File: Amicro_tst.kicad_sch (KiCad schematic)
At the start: 19 parts, among them J1 Conn_01x04_Female, J2 Conn_01x05_Female, J3 Conn_01x04_Female, SW1 SW_Push, U1 ATmega328-P, U2 24LC512, Y1 Crystal

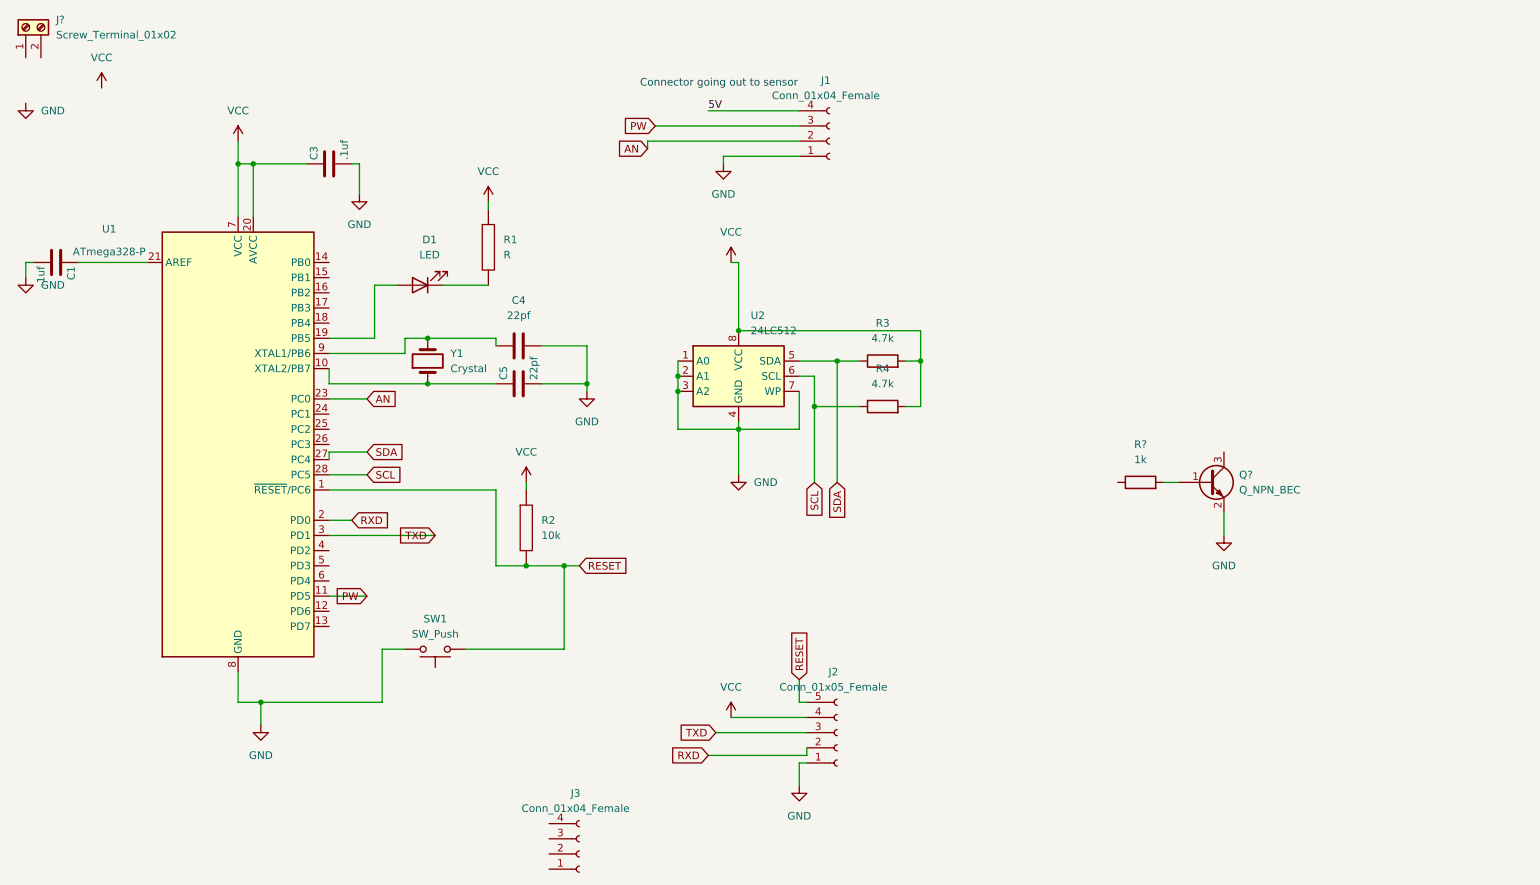
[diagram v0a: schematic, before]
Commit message: redid lost work/testpoints
Redid lost work that didnt save, still need to find footprints for transistors
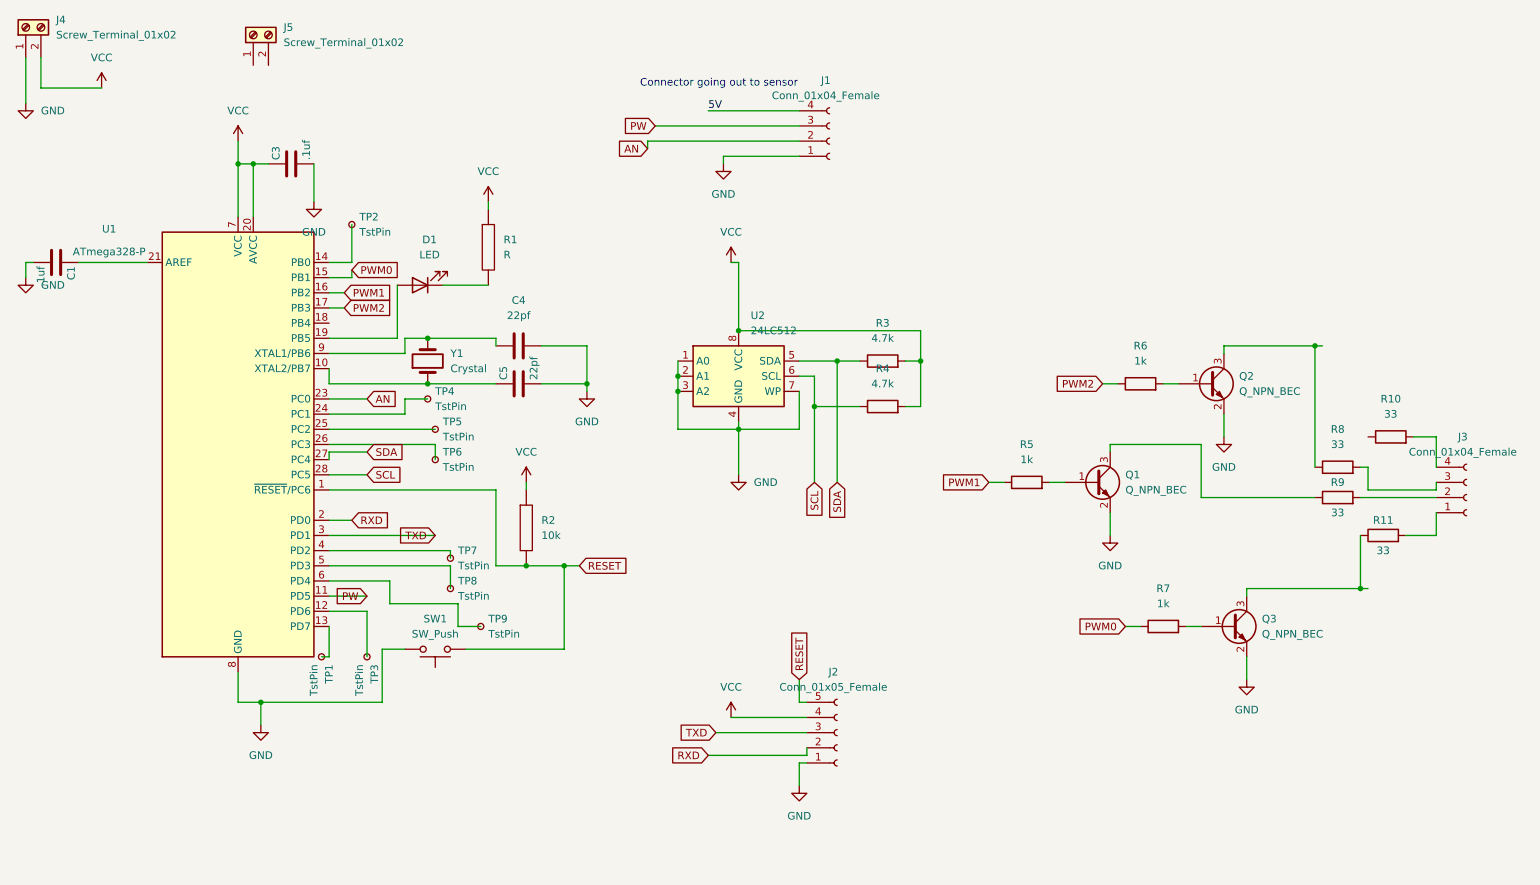
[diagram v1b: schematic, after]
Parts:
- added J5: Screw_Terminal_01x02, symbol Connector:Screw_Terminal_01x02
- added Q2, Q3: Q_NPN_BEC, symbol Device:Q_NPN_BEC
- added R10, R11, R8, R9: 33, Resistor_SMD:R_0402_1005Metric, symbol Device:R
- added R6, R7: 1k, Resistor_SMD:R_0402_1005Metric, symbol Device:R
- added TP1, TP2, TP3, TP4, TP5, TP6, TP7, TP8, TP9: TstPin, TestPoint:TestPoint_THTPad_1.0x1.0mm_Drill0.5mm, symbol Connector:TestPoint_Small
- J4: renamed from J?; footprint (none) -> TerminalBlock_4Ucon:TerminalBlock_4Ucon_1x02_P3.50mm_Vertical
- gave numbers to parts that had none: 2
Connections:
- net GND: now also J4.1 (Pin_1), Q2.2 (E), Q3.2 (E)
- net VCC: now also J4.2 (Pin_2)
- net at Q1.3 (C): now also R9.1
- net PWM1: now reaches R5.1
- net PWM1: now also U1.16 (PB2)
- net at U1.12 (PD6): now also TP3.1
- net at U1.13 (PD7): now also TP1.1
- net at U1.14 (PB0): now also TP2.1
- net PWM0: now reaches U1.15 (PB1)
- net PWM0: now also R7.1
- net PWM2: now reaches U1.17 (PB3)
- net PWM2: now also R6.1
- net at U1.24 (PC1): now also TP4.1
- net at U1.25 (PC2): now also TP5.1
- net at U1.26 (PC3): now also TP6.1
- net at U1.4 (PD2): now also TP7.1
- net at U1.5 (PD3): now also TP8.1
- net at U1.6 (PD4): now also TP9.1
- net at J3.1 (Pin_1): now also R11.2
- net at J3.2 (Pin_2): now also R9.2
- net at J3.3 (Pin_3): now also R8.2
- net at J3.4 (Pin_4): now also R10.2
- new net: Q2.3 (C), R8.1
- new net: Q2.1 (B), R6.2
- new net: Q3.1 (B), R7.2
- new net: Q3.3 (C), R11.1
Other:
- moved on the sheet: C3, J3, Q1, R5

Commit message: transistor footprints
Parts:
- J1: footprint Connector_PinSocket_1.00mm:PinSocket_1x05_P1.00mm_Vertical -> Connector_JST:JST_EH_S4B-EH_1x04_P2.50mm_Horizontal
- Q1: footprint (none) -> Package_TO_SOT_SMD:SC-59_Handsoldering
- Q2, Q3: footprint (none) -> TO_SOT_Packages_SMD:SC-59_Handsoldering
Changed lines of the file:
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@@
       (effects (font (size 1.27 1.27)) (justify left))
     )
-    (property "Footprint" "" (id 2) (at 214.63 116.84 0)
+    (property "Footprint" "Package_TO_SOT_SMD:SC-59_Handsoldering" (id 2) (at 214.63 116.84 0)
       (effects (font (size 1.27 1.27)) hide)
     )
@@
     (property "Reference" "J1" (id 0) (at 164.465 52.07 0))
     (property "Value" "Conn_01x04_Female" (id 1) (at 164.465 54.61 0))
-    (property "Footprint" "Connector_PinSocket_1.00mm:PinSocket_1x05_P1.00mm_Vertical" (id 2) (at 165.1 62.23 0)
+    (property "Footprint" "Connector_JST:JST_EH_S4B-EH_1x04_P2.50mm_Horizontal" (id 2) (at 165.1 62.23 0)
       (effects (font (size 1.27 1.27)) hide)
     )
@@
       (effects (font (size 1.27 1.27)) (justify left))
     )
-    (property "Footprint" "" (id 2) (at 233.68 100.33 0)
+    (property "Footprint" "TO_SOT_Packages_SMD:SC-59_Handsoldering" (id 2) (at 233.68 100.33 0)
       (effects (font (size 1.27 1.27)) hide)
     )
@@
       (effects (font (size 1.27 1.27)) (justify left))
     )
-    (property "Footprint" "" (id 2) (at 237.49 140.97 0)
+    (property "Footprint" "TO_SOT_Packages_SMD:SC-59_Handsoldering" (id 2) (at 237.49 140.97 0)
       (effects (font (size 1.27 1.27)) hide)
     )
@@
     )
     (path "/5188af90-2c2e-4efc-b1a8-f03acba966ff"
-      (reference "J1") (unit 1) (value "Conn_01x04_Female") (footprint "Connector_PinSocket_1.00mm:PinSocket_1x05_P1.00mm_Vertical")
+      (reference "J1") (unit 1) (value "Conn_01x04_Female") (footprint "Connector_JST:JST_EH_S4B-EH_1x04_P2.50mm_Horizontal")
     )
     (path "/fabc0f20-6748-4256-8270-8d8c1ba7f1db"
@@
     )
     (path "/2040b5f2-deb5-43fd-af37-1d21e87e6c5d"
-      (reference "Q1") (unit 1) (value "Q_NPN_BEC") (footprint "")
+      (reference "Q1") (unit 1) (value "Q_NPN_BEC") (footprint "Package_TO_SOT_SMD:SC-59_Handsoldering")
     )
     (path "/554d6924-f0a1-44e8-9c6e-2df61b13682e"
-      (reference "Q2") (unit 1) (value "Q_NPN_BEC") (footprint "")
+      (reference "Q2") (unit 1) (value "Q_NPN_BEC") (footprint "TO_SOT_Packages_SMD:SC-59_Handsoldering")
     )
     (path "/c9e48f35-9002-4ee0-bbbf-ca80e2ff2954"
-      (reference "Q3") (unit 1) (value "Q_NPN_BEC") (footprint "")
+      (reference "Q3") (unit 1) (value "Q_NPN_BEC") (footprint "TO_SOT_Packages_SMD:SC-59_Handsoldering")
     )
     (path "/2719589e-6f3e-41f2-ae58-0c107b009320"

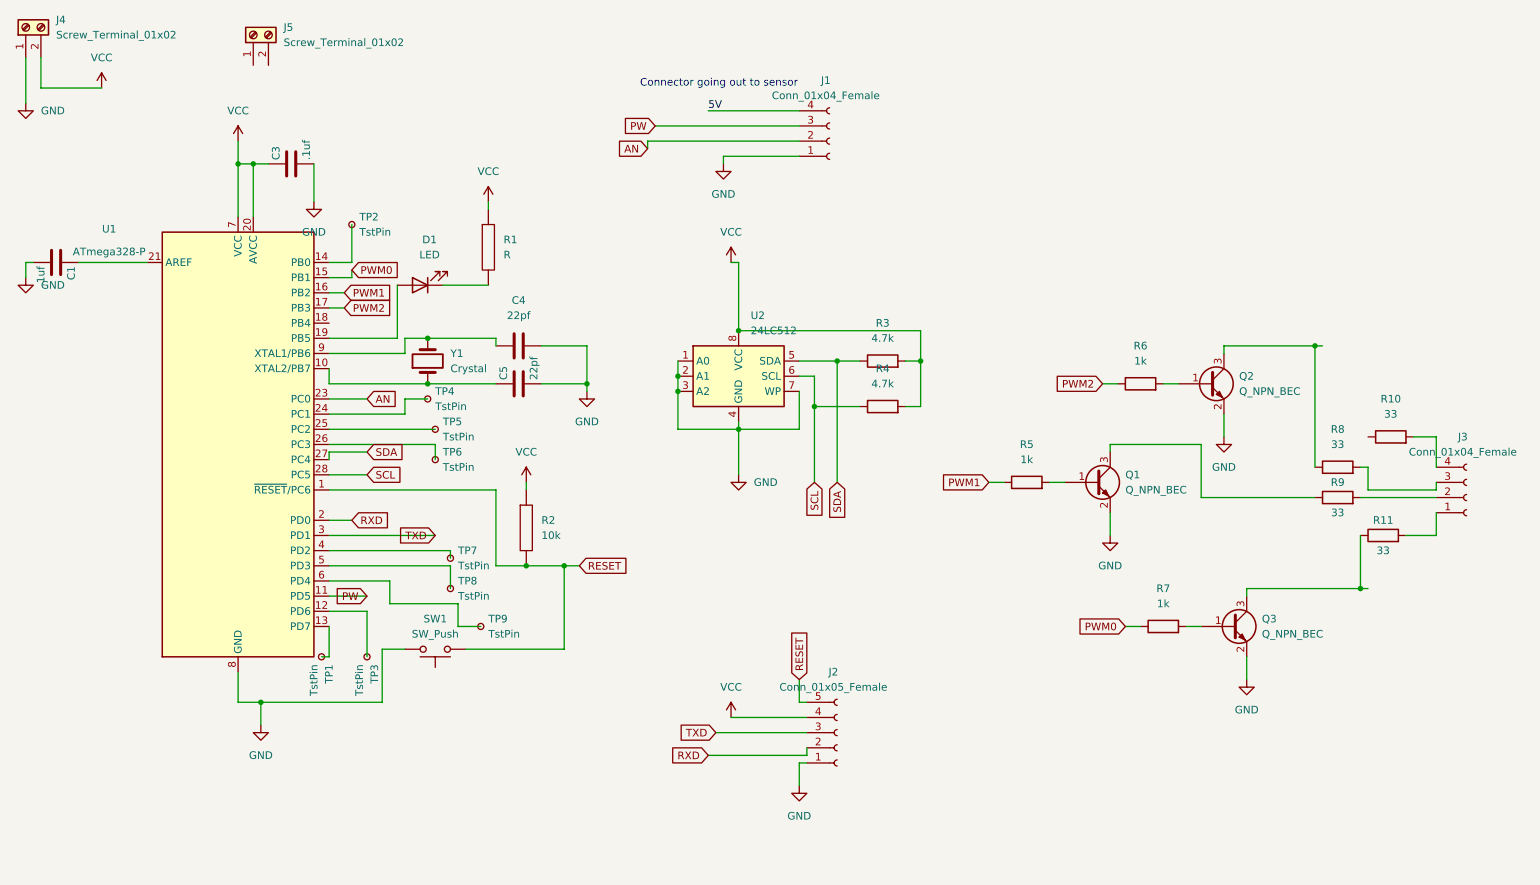
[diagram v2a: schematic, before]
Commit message: Changed Footprints & Board Size
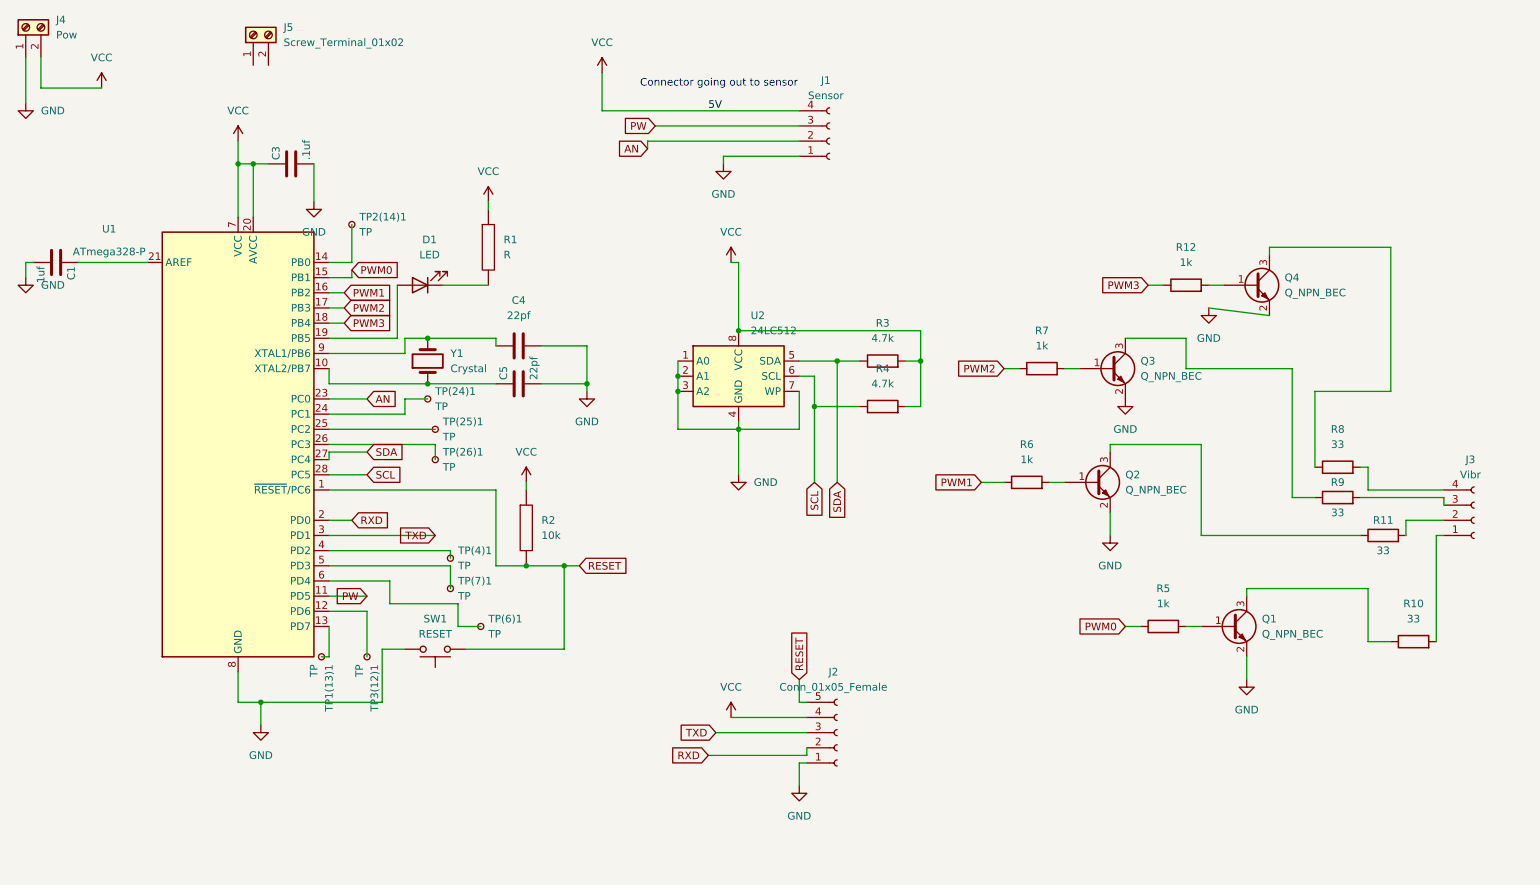
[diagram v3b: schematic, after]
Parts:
- added Q4: Q_NPN_BEC, Package_TO_SOT_SMD:SC-59_Handsoldering, symbol Device:Q_NPN_BEC
- added R12: 1k, Resistor_SMD:R_0402_1005Metric, symbol Device:R
- J1: value Conn_01x04_Female -> Sensor
- J3: value Conn_01x04_Female -> Vibr; footprint Connector_JST:JST_EH_S4B-EH_1x04_P2.50mm_Horizontal -> Connector_PinSocket_1.00mm:PinSocket_1x04_P1.00mm_Vertical
- J4: value Screw_Terminal_01x02 -> Pow; footprint TerminalBlock_4Ucon:TerminalBlock_4Ucon_1x02_P3.50mm_Vertical -> TestPoint:TestPoint_2Pads_Pitch5.08mm_Drill1.3mm
- Q1: renamed from Q3; footprint TO_SOT_Packages_SMD:SC-59_Handsoldering -> Package_TO_SOT_SMD:SC-59_Handsoldering
- Q3: renamed from Q2; footprint TO_SOT_Packages_SMD:SC-59_Handsoldering -> Package_TO_SOT_SMD:SC-59_Handsoldering
- SW1: value SW_Push -> RESET
- TP(24)1: renamed from TP4; value TstPin -> TP
- TP(25)1: renamed from TP5; value TstPin -> TP
- TP(26)1: renamed from TP6; value TstPin -> TP
- TP(4)1: renamed from TP7; value TstPin -> TP
- TP(6)1: renamed from TP9; value TstPin -> TP
- TP(7)1: renamed from TP8; value TstPin -> TP
- TP1(13)1: renamed from TP1; value TstPin -> TP
- TP2(14)1: renamed from TP2; value TstPin -> TP
- TP3(12)1: renamed from TP3; value TstPin -> TP
- renumbered Q1 to Q2, R7 to R5, R5 to R6, R6 to R7
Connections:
- net 5V is gone; now on net VCC: J1.4 (Pin_4)
- net GND: now also Q4.2 (E)
- net at Q2.3 (C): now also R11.1; no longer R9.1
- net at R8.1: now also Q4.3 (C); no longer Q3.3 (C)
- net at R8.2: now also J3.4 (Pin_4); no longer J3.3 (Pin_3)
- net at R9.2: now also J3.3 (Pin_3); no longer J3.2 (Pin_2)
- net PWM3: now reaches U1.18 (PB4)
- net PWM3: now also R12.1
- net at J3.1 (Pin_1): now also R10.2; no longer R11.2
- net at R10.1: now also Q1.3 (C)
- new net: Q4.1 (B), R12.2
- new net: Q3.3 (C), R9.1
- new net: J3.2 (Pin_2), R11.2
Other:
- moved on the sheet: J3, Q3, R10, R7
